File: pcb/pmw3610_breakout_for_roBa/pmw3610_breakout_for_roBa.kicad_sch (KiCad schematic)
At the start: 13 parts, among them J1 Conn_01x08, U1 MCP1700T-1802E/TT, U2 PMW3610

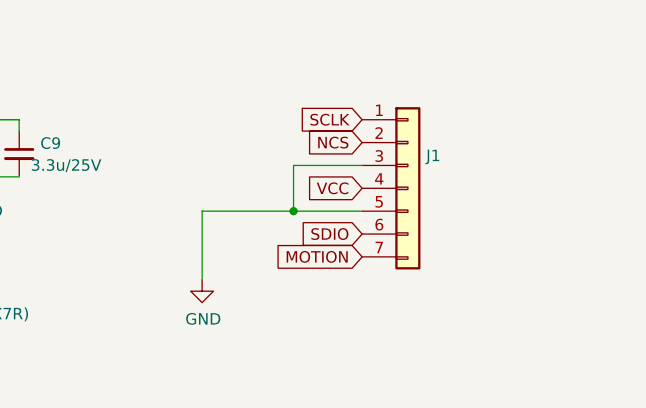
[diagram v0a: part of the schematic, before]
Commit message: Add VIK connector to trackball PCB, Remove earlier revisions
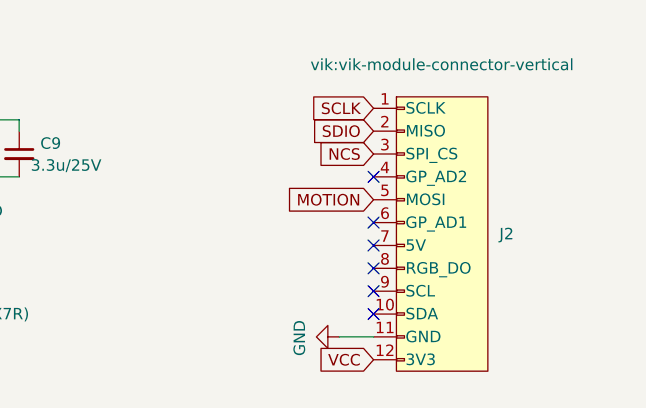
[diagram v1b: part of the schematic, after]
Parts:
- removed J1: Conn_01x08, roBa:pmw3610_connector_b, symbol Connector_Generic:Conn_01x06
- added J2: vik-module-connector, vik:vik-module-connector-vertical, symbol vik:vik-module-connector
- C5: value 100n (X7R) -> 100n (X7R)
- C6: value 10u (X7R) -> 10u (X7R)
- C7: value 10n (X7R) -> 10n (X7R)
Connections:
- net GND: now also J2.11 (GND)
- net MOTION: now also J2.5 (MOSI)
- net NCS: now also J2.3 (SPI_CS)
- net SCLK: now also J2.1 (SCLK)
- net SDIO: now also J2.2 (MISO)
- net VCC: now also J2.12 (3V3)
- no-connect marks 0 -> 6
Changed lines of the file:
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@@
 	(paper "A4")
-	(junction
-		(at 219.71 101.6)
-		(diameter 0)
-		(color 0 0 0 0)
-	)
 	(junction
 		(at 181.61 91.44)
@@
 		(color 0 0 0 0)
 	)
+	(no_connect
+		(at 228.6 102.87)
+	)
+	(no_connect
+		(at 228.6 113.03)
+	)
+	(no_connect
+		(at 228.6 97.79)
+	)
+	(no_connect
+		(at 228.6 105.41)
+	)
+	(no_connect
+		(at 228.6 110.49)
+	)
+	(no_connect
+		(at 228.6 107.95)
+	)
 	(wire
 		(pts
@@
 	(wire
 		(pts
-			(xy 227.33 101.6) (xy 219.71 101.6)
+			(xy 224.79 115.57) (xy 228.6 115.57)
 		)
 		(stroke
@@
 	(wire
 		(pts
-			(xy 219.71 101.6) (xy 219.71 96.52)
-		)
-		(stroke
-			(width 0)
-			(type default)
-		)
-	)
-	(wire
-		(pts
 			(xy 114.554 105.41) (xy 129.54 105.41)
 		)
@@
 	(wire
 		(pts
-			(xy 209.55 101.6) (xy 219.71 101.6)
-		)
-		(stroke
-			(width 0)
-			(type default)
-		)
-	)
-	(wire
-		(pts
 			(xy 105.41 102.87) (xy 109.22 102.87)
 		)
@@
 	(wire
 		(pts
-			(xy 219.71 96.52) (xy 227.33 96.52)
-		)
-		(stroke
-			(width 0)
-			(type default)
-		)
-	)
-	(wire
-		(pts
 			(xy 165.1 82.55) (xy 127 82.55)
 		)
@@
 		(pts
 			(xy 49.53 93.98) (xy 57.15 93.98)
-		)
-		(stroke
-			(width 0)
-			(type default)
-		)
-	)
-	(wire
-		(pts
-			(xy 209.55 101.6) (xy 209.55 109.22)
 		)
 		(stroke
@@
 	(global_label "MOTION"
 		(shape input)
-		(at 227.33 106.68 180)
+		(at 228.6 100.33 180)
 		(fields_autoplaced yes)
 		(effects
@@
 		)
 		(property "Intersheetrefs" "${INTERSHEET_REFS}"
-			(at 217.3295 106.68 0)
+			(at 218.5995 100.33 0)
 			(effects
 				(font
@@
 	(global_label "NCS"
 		(shape input)
-		(at 227.33 93.98 180)
+		(at 228.6 95.25 180)
 		(fields_autoplaced yes)
 		(effects
@@
 		)
 		(property "Intersheetrefs" "${INTERSHEET_REFS}"
-			(at 220.5348 93.98 0)
+			(at 221.8048 95.25 0)
 			(effects
 				(font
@@
 	(global_label "SCLK"
 		(shape input)
-		(at 227.33 91.44 180)
+		(at 228.6 90.17 180)
 		(fields_autoplaced yes)
 		(effects
@@
 		)
 		(property "Intersheetrefs" "${INTERSHEET_REFS}"
-			(at 219.5672 91.44 0)
+			(at 220.8372 90.17 0)
 			(effects
 				(font
@@
 	(global_label "SDIO"
 		(shape input)
-		(at 227.33 104.14 180)
+		(at 228.6 92.71 180)
 		(fields_autoplaced yes)
 		(effects
@@
 		)
 		(property "Intersheetrefs" "${INTERSHEET_REFS}"
-			(at 219.93 104.14 0)
+			(at 221.2 92.71 0)
 			(effects
 				(font
@@
 	(global_label "VCC"
 		(shape input)
-		(at 227.33 99.06 180)
+		(at 228.6 118.11 180)
 		(fields_autoplaced yes)
 		(effects
@@
 		)
 		(property "Intersheetrefs" "${INTERSHEET_REFS}"
-			(at 221.2883 99.1394 0)
+			(at 222.5583 118.1894 0)
 			(effects
 				(font
@@
 				(path "/b4729a3c-d911-404a-9272-8567e8114e1c"
 					(reference "U2")
-					(unit 1)
-				)
-			)
-		)
-	)
-	(symbol
-		(lib_id "Connector_Generic:Conn_01x06")
-		(at 232.41 96.52 0)
-		(unit 1)
-		(exclude_from_sim no)
-		(in_bom yes)
-		(on_board yes)
-		(dnp no)
-		(property "Reference" "J1"
-			(at 234.442 95.4532 0)
-			(effects
-				(font
-					(size 1.27 1.27)
-				)
-				(justify left)
-			)
-		)
-		(property "Value" "Conn_01x08"
-			(at 234.442 97.7646 0)
-			(effects
-				(font
-					(size 1.27 1.27)
-				)
-				(justify left)
-				(hide yes)
-			)
-		)
-		(property "Footprint" "roBa:pmw3610_connector_b"
-			(at 232.41 96.52 0)
-			(effects
-				(font
-					(size 1.27 1.27)
-				)
-				(hide yes)
-			)
-		)
-		(property "Datasheet" "~"
-			(at 232.41 96.52 0)
-			(effects
-				(font
-					(size 1.27 1.27)
-				)
-				(hide yes)
-			)
-		)
-		(property "Description" ""
-			(at 232.41 96.52 0)
-			(effects
-				(font
-					(size 1.27 1.27)
-				)
-				(hide yes)
-			)
-		)
-		(pin "1"
-		)
-		(pin "2"
-		)
-		(pin "3"
-		)
-		(pin "4"
-		)
-		(pin "5"
-		)
-		(pin "6"
-		)
-		(pin "7"
-		)
-		(instances
-			(project "pmw3610_breakout_for_roBa"
-				(path "/b4729a3c-d911-404a-9272-8567e8114e1c"
-					(reference "J1")
 					(unit 1)
 				)
@@
 	(symbol
 		(lib_id "power:GND")
-		(at 209.55 109.22 0)
+		(at 224.79 115.57 270)
 		(unit 1)
 		(exclude_from_sim no)
@@
 		(dnp no)
 		(property "Reference" "#PWR07"
-			(at 209.55 115.57 0)
+			(at 218.44 115.57 0)
 			(effects
 				(font
@@
 		)
 		(property "Value" "GND"
-			(at 209.677 113.6142 0)
+			(at 220.3958 115.697 0)
 			(effects
 				(font
@@
 		)
 		(property "Footprint" ""
-			(at 209.55 109.22 0)
+			(at 224.79 115.57 0)
 			(effects
 				(font
@@
 		)
 		(property "Datasheet" ""
-			(at 209.55 109.22 0)
+			(at 224.79 115.57 0)
 			(effects
 				(font
@@
 		)
 		(property "Description" ""
-			(at 209.55 109.22 0)
+			(at 224.79 115.57 0)
 			(effects
 				(font
@@
 			)
 		)
-		(property "Value" " 100n (X7R)"
+		(property "Value" "100n (X7R)"
 			(at 166.37 100.33 0)
 			(effects
@@
 			)
 		)
-		(property "Value" " 10n (X7R)"
+		(property "Value" "10n (X7R)"
 			(at 181.61 113.03 0)
 			(effects
@@
 			)
 		)
-		(property "Value" " 10u (X7R)"
+		(property "Value" "10u (X7R)"
 			(at 171.45 113.03 0)
 			(effects
@@
 					(unit 1)
 				)
+			)
+		)
+	)
+	(symbol
+		(lib_id "vik:vik-module-connector")
+		(at 236.22 102.87 0)
+		(unit 1)
+		(exclude_from_sim no)
+		(in_bom yes)
+		(on_board yes)
+		(dnp no)
+		(property "Reference" "J2"
+			(at 242.57 104.1399 0)
+			(effects
+				(font
+					(size 1.27 1.27)
+				)
+				(justify left)
+			)
+		)
+		(property "Value" "vik-module-connector"
+			(at 236.22 120.65 0)
+			(effects
+				(font
+					(size 1.27 1.27)
+				)
+				(hide yes)
+			)
+		)
+		(property "Footprint" "vik:vik-module-connector-vertical"
+			(at 236.22 85.344 0)
+			(effects
+				(font
+					(size 1.27 1.27)
+				)
+			)
+		)
+		(property "Datasheet" ""
+			(at 236.22 96.52 0)
+			(effects
+				(font
+					(size 1.27 1.27)
+				)
+				(hide yes)
+			)
+		)
+		(property "Description" ""
+			(at 236.22 102.87 0)
+			(effects
+				(font
+					(size 1.27 1.27)
+				)
+				(hide yes)
+			)
+		)
+		(pin "11"
+		)
+		(pin "3"
+		)
+		(pin "1"
+		)
+		(pin "10"
+		)
+		(pin "12"
+		)
+		(pin "2"
+		)
+		(pin "4"
+		)
+		(pin "5"
+		)
+		(pin "6"
+		)
+		(pin "7"
+		)
+		(pin "8"
+		)
+		(pin "9"
+		)
+		(instances
+			(project ""
+				(path "/b4729a3c-d911-404a-9272-8567e8114e1c"
+					(reference "J2")
+					(unit 1)
+				)

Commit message: Update pmw3610 breakout
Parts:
- C1: value 1u -> 0.1uF; LCSC C14663 -> (none)
- C2: value 1u -> 1uF; LCSC C15849 -> (none)
- C3, C8: value 100n -> 100nF; LCSC C19666 -> (none)
- C4: LCSC C19666 -> (none)
- C6: value 10u (X7R) -> 10uF (X7R); LCSC C19666 -> (none)
- C7: value 10n (X7R) -> 10nF (X7R); LCSC C19666 -> (none)
- C9: value 3.3u/25V -> 3.3uF/16V; LCSC C19666 -> (none)
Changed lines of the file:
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@@
 			)
 		)
-		(property "Value" "1u"
+		(property "Value" "1uF"
 			(at 82.3468 97.663 0)
 			(effects
@@
 		)
 		(property "Description" ""
-			(at 80.01 96.52 0)
-			(effects
-				(font
-					(size 1.27 1.27)
-				)
-				(hide yes)
-			)
-		)
-		(property "LCSC" "C15849"
 			(at 80.01 96.52 0)
 			(effects
@@
 		(lib_id "Device:C_Small")
 		(at 109.22 105.41 0)
+		(mirror y)
 		(unit 1)
 		(exclude_from_sim no)
@@
 		(dnp no)
 		(property "Reference" "C3"
-			(at 111.5568 104.2416 0)
-			(effects
-				(font
-					(size 1.27 1.27)
-				)
-				(justify left)
-			)
-		)
-		(property "Value" "100n"
-			(at 111.5568 106.553 0)
+			(at 106.8832 104.2416 0)
+			(effects
+				(font
+					(size 1.27 1.27)
+				)
+				(justify left)
+			)
+		)
+		(property "Value" "100nF"
+			(at 106.8832 106.553 0)
 			(effects
 				(font
@@
 		)
 		(property "Description" ""
-			(at 109.22 105.41 0)
-			(effects
-				(font
-					(size 1.27 1.27)
-				)
-				(hide yes)
-			)
-		)
-		(property "LCSC" "C19666"
 			(at 109.22 105.41 0)
 			(effects
@@
 			)
 		)
-		(property "Value" "100n"
+		(property "Value" "100nF"
 			(at 180.34 96.52 0)
 			(effects
@@
 			)
 		)
-		(property "LCSC" "C19666"
-			(at 181.61 95.25 0)
-			(effects
-				(font
-					(size 1.27 1.27)
-				)
-				(hide yes)
-			)
-		)
 		(pin "1"
 		)
@@
 		)
 		(property "Description" ""
-			(at 165.1 85.09 0)
-			(effects
-				(font
-					(size 1.27 1.27)
-				)
-				(hide yes)
-			)
-		)
-		(property "LCSC" "C19666"
 			(at 165.1 85.09 0)
 			(effects
@@
 			)
 		)
-		(property "Value" "1u"
+		(property "Value" "0.1uF"
 			(at 54.8386 97.663 0)
 			(effects
@@
 			)
 		)
-		(property "LCSC" "C14663"
-			(at 57.15 96.52 0)
-			(effects
-				(font
-					(size 1.27 1.27)
-				)
-				(hide yes)
-			)
-		)
 		(pin "1"
 		)
@@
 			)
 		)
-		(property "Value" "10n (X7R)"
+		(property "Value" "10nF (X7R)"
 			(at 181.61 113.03 0)
 			(effects
@@
 			)
 		)
-		(property "LCSC" "C19666"
-			(at 180.34 111.76 0)
-			(effects
-				(font
-					(size 1.27 1.27)
-				)
-				(hide yes)
-			)
-		)
 		(pin "1"
 		)
@@
 			)
 		)
-		(property "Value" "3.3u/25V"
+		(property "Value" "3.3uF/16V"
 			(at 190.5 96.52 0)
 			(effects
@@
 		)
 		(property "Description" ""
-			(at 189.23 95.25 0)
-			(effects
-				(font
-					(size 1.27 1.27)
-				)
-				(hide yes)
-			)
-		)
-		(property "LCSC" "C19666"
 			(at 189.23 95.25 0)
 			(effects
@@
 			)
 		)
-		(property "Value" "10u (X7R)"
+		(property "Value" "10uF (X7R)"
 			(at 171.45 113.03 0)
 			(effects
@@
 			(at 172.72 111.76 0)
 			(effects
-				(font
-					(size 1.27 1.27)
-				)
-				(hide yes)
-			)
-		)
-		(property "LCSC" "C19666"
-			(at 172.72 111.76 0)
-			(effects

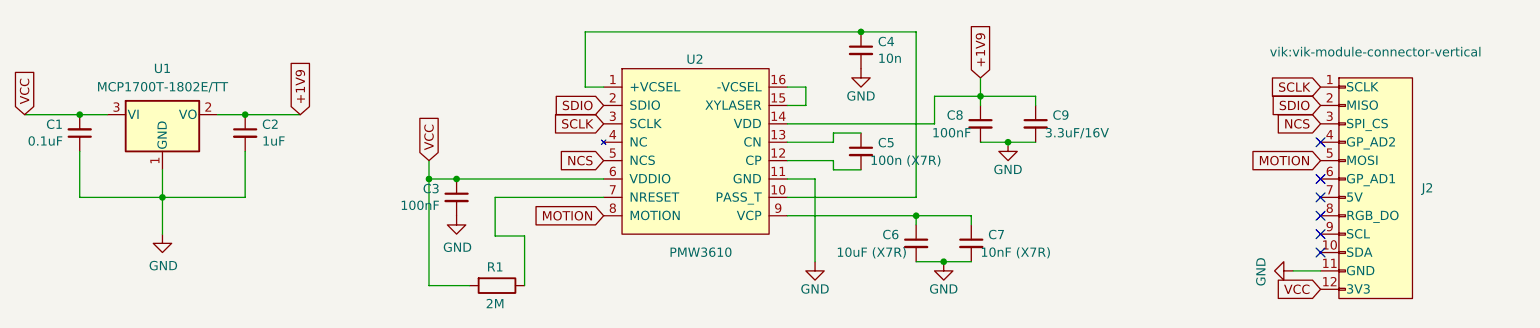
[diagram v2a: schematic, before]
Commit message: Change C1 value according to datasheet
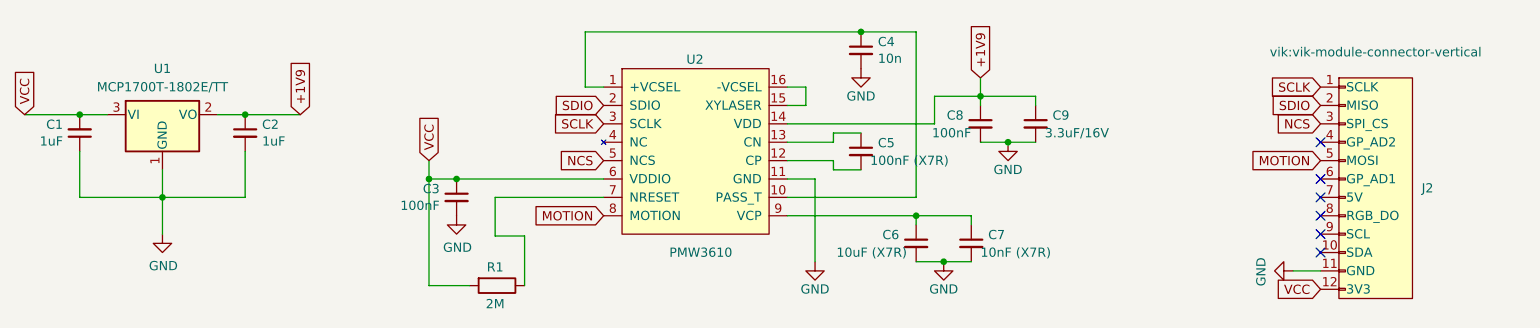
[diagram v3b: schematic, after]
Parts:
- C1: value 0.1uF -> 1uF
- C5: value 100n (X7R) -> 100nF (X7R)
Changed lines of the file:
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@@
 			)
 		)
-		(property "Value" "100n (X7R)"
+		(property "Value" "100nF (X7R)"
 			(at 166.37 100.33 0)
 			(effects
@@
 			)
 		)
-		(property "Value" "0.1uF"
+		(property "Value" "1uF"
 			(at 54.8386 97.663 0)
 			(effects

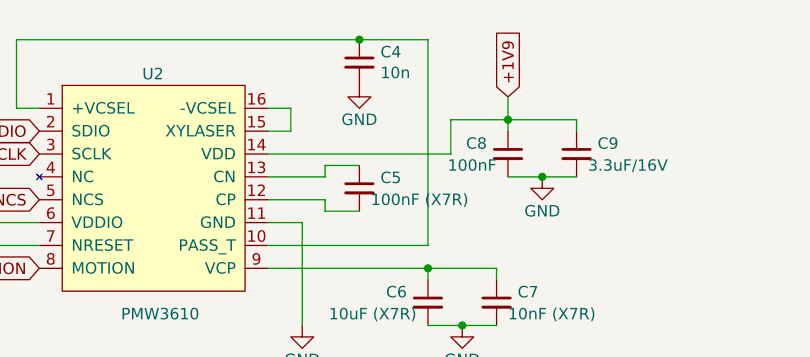
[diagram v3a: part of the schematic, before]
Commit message: Fix capacitor values and generate production files
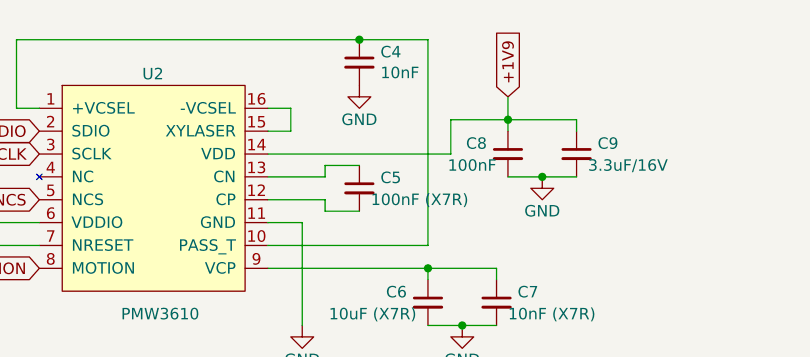
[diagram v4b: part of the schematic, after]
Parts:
- C4: value 10n -> 10nF
- C5: LCSC C19666 -> (none)
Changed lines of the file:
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@@
 			)
 		)
-		(property "Value" "10n"
+		(property "Value" "10nF"
 			(at 167.4368 86.233 0)
 			(effects
@@
 			(at 165.1 99.06 0)
 			(effects
-				(font
-					(size 1.27 1.27)
-				)
-				(hide yes)
-			)
-		)
-		(property "LCSC" "C19666"
-			(at 165.1 99.06 0)
-			(effects
